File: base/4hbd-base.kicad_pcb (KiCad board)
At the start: 2 copper layers, 155 parts, among them J13 Conn_01x08, J14 Conn_02x25_Odd_Even, J15 Conn_02x25_Odd_Even, Q1 irf540n, Q10 2N7002, Q2 irf540n, Q3 irf540n, Q4 irf540n, Q5 irf540n, Q6 irf540n, Q7 irf540n, Q8 irf540n, Q9 2N7002, U1 SI8640, U10 ADS7886, U11 MOCD217M, U12 MOCD217M, U13 MOCD217M, U14 AMS1117-5.0, U15 AMS1117-5.0, U16 AMS1117-3.3, U17 LM2596S-ADJ, U18 AM26LV32, U19 LM2596S-ADJ, U2 SI8640, U20 AMS1117-5.0, U21 SN65HVD230, U3 IR2181, U4 IR2181, U5 IR2181, U6 IR2181, U7 ACS712xLCTR-30A, U8 ACS712xLCTR-30A, U9 ADS7886

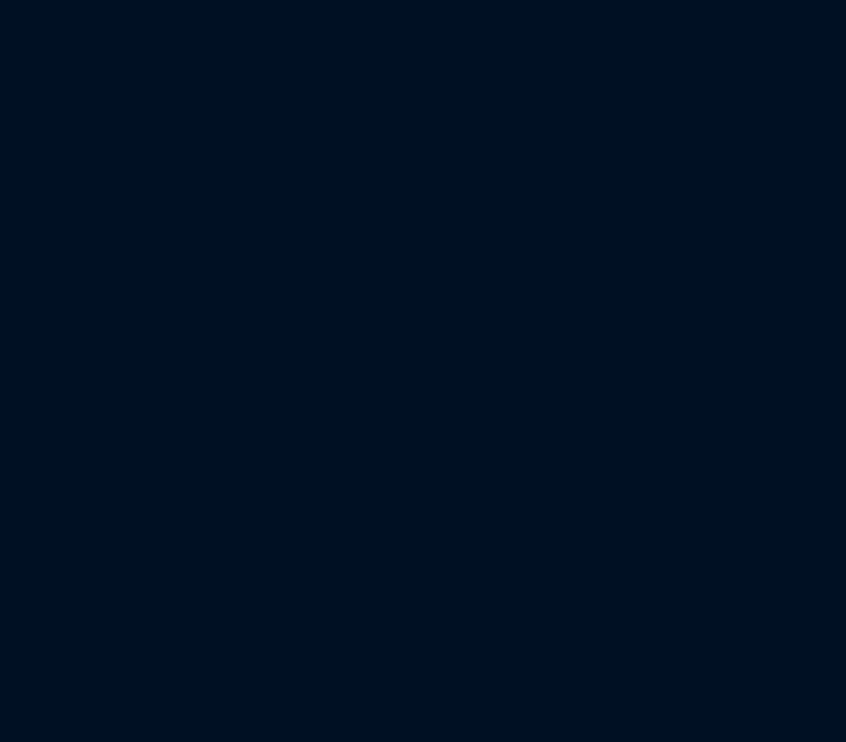
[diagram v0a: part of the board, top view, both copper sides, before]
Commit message: added footprints, created netlist
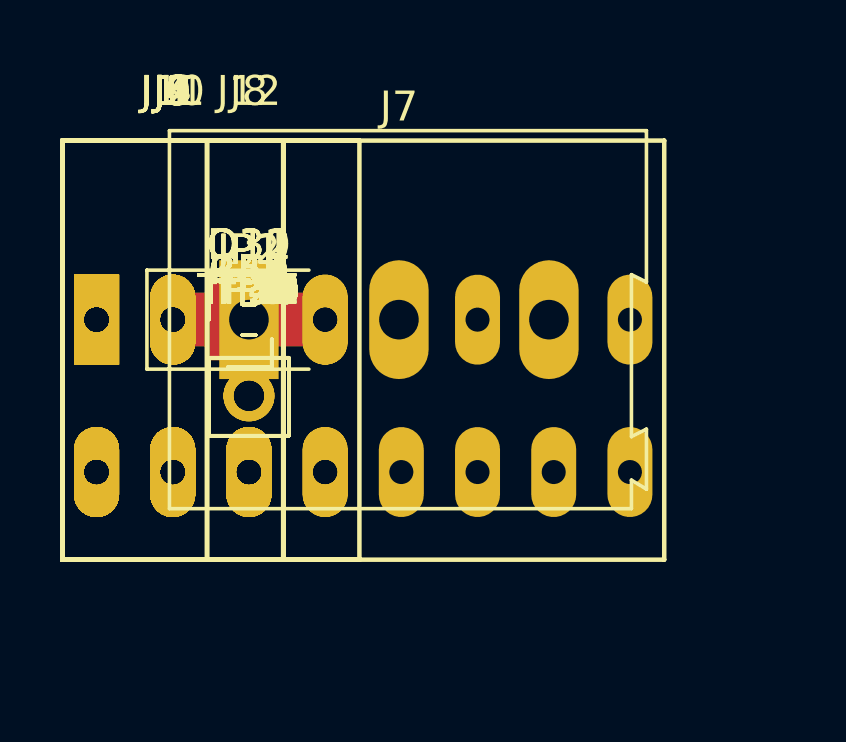
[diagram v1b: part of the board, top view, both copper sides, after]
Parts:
- added C42, C43: 0.1uF, Capacitor_SMD:C_0603_1608Metric, F.Cu at (0.00, 0.00)
- added D30: 1N5822, Diode_SMD:D_SMA, F.Cu at (0.00, 0.00)
- added D31: NUP2105L, Package_TO_SOT_SMD:SOT-23, F.Cu at (0.00, 0.00)
- added J1, J10, J11, J2, J3, J4, J9: Spring_Terminal_Connector_01x03, TerminalBlock:SpringTerminalBlock_KF141R_3_P2.54mm, F.Cu at (0.00, 0.00)
- added J12: Spring_Terminal_Connector_01x08, TerminalBlock:SpringTerminalBlock_KF141R_8_P2.54mm, F.Cu at (0.00, 0.00)
- added J5, J6: Spring_Terminal_Connector_01x02, TerminalBlock:SpringTerminalBlock_KF141R_2_P2.54mm, F.Cu at (0.00, 0.00)
- added J7: Screw_Terminal_01x03, TerminalBlock:TerminalBlock_Altech_AK300-3_P5.00mm, F.Cu at (0.00, 0.00)
- added J8: Spring_Terminal_Connector_01x04, TerminalBlock:SpringTerminalBlock_KF141R_4_P2.54mm, F.Cu at (0.00, 0.00)
- added JP1, JP2: Jumper_NC_Small, Connector_PinHeader_2.54mm:PinHeader_1x02_P2.54mm_Vertical, F.Cu at (0.00, 0.00)
- added Q11: 2N7002, Package_TO_SOT_SMD:SOT-23, F.Cu at (0.00, 0.00)
- added Q12: IRLML2060TRPBF, Package_TO_SOT_SMD:SOT-23, F.Cu at (0.00, 0.00)
- added R44: 10k, Resistor_SMD:R_0603_1608Metric, F.Cu at (0.00, 0.00)
- added R45: 2K2, Resistor_SMD:R_0603_1608Metric, F.Cu at (0.00, 0.00)
- added R46, R51: 10K, Resistor_SMD:R_0603_1608Metric, F.Cu at (0.00, 0.00)
- added R47, R48, R49, R54, R55: 120, Resistor_SMD:R_0603_1608Metric, F.Cu at (0.00, 0.00)
- added R50: 1K, Resistor_SMD:R_0603_1608Metric, F.Cu at (0.00, 0.00)
- added R52: 360, Resistor_SMD:R_0603_1608Metric, F.Cu at (0.00, 0.00)
- added R53: 100, Resistor_SMD:R_0603_1608Metric, F.Cu at (0.00, 0.00)
- added TP1, TP2, TP3, TP4, TP5: GNDp, TestPoint:TestPoint_Pad_D1.5mm, F.Cu at (0.00, 0.00)
- added TP10: PWM1p, TestPoint:TestPoint_Pad_D1.5mm, F.Cu at (0.00, 0.00)
- added TP11: PWM1n, TestPoint:TestPoint_Pad_D1.5mm, F.Cu at (0.00, 0.00)
- added TP12: PWM2p, TestPoint:TestPoint_Pad_D1.5mm, F.Cu at (0.00, 0.00)
- added TP13: PWM2n, TestPoint:TestPoint_Pad_D1.5mm, F.Cu at (0.00, 0.00)
- added TP14: PWM3p, TestPoint:TestPoint_Pad_D1.5mm, F.Cu at (0.00, 0.00)
- added TP15: PWM3n, TestPoint:TestPoint_Pad_D1.5mm, F.Cu at (0.00, 0.00)
- added TP16, TP17, TP18, TP19, TP20: GNDd, TestPoint:TestPoint_Pad_D1.5mm, F.Cu at (0.00, 0.00)
- added TP27: driver_VB, TestPoint:TestPoint_Pad_D1.5mm, F.Cu at (0.00, 0.00)
- added TP28: driver_VS, TestPoint:TestPoint_Pad_D1.5mm, F.Cu at (0.00, 0.00)
- added TP29: driver_HO, TestPoint:TestPoint_Pad_D1.5mm, F.Cu at (0.00, 0.00)
- added TP30: +24Vd_IN, TestPoint:TestPoint_Pad_D1.5mm, F.Cu at (0.00, 0.00)
- added TP31: +5Vd_main, TestPoint:TestPoint_Pad_D1.5mm, F.Cu at (0.00, 0.00)
- added TP32: +5Vd_enc, TestPoint:TestPoint_Pad_D1.5mm, F.Cu at (0.00, 0.00)
- added TP33: +24Vd_OUT, TestPoint:TestPoint_Pad_D1.5mm, F.Cu at (0.00, 0.00)
- added TP34: +6.8Vd, TestPoint:TestPoint_Pad_D1.5mm, F.Cu at (0.00, 0.00)
- added TP35: +24Vp_IN, TestPoint:TestPoint_Pad_D1.5mm, F.Cu at (0.00, 0.00)
- added TP36: +12Vp, TestPoint:TestPoint_Pad_D1.5mm, F.Cu at (0.00, 0.00)
- added TP37: +5Vp, TestPoint:TestPoint_Pad_D1.5mm, F.Cu at (0.00, 0.00)
- added TP38: CAN_Tx, TestPoint:TestPoint_Pad_D1.5mm, F.Cu at (0.00, 0.00)
- added TP39: CAN_Rx, TestPoint:TestPoint_Pad_D1.5mm, F.Cu at (0.00, 0.00)
- added TP40: 485_Tx, TestPoint:TestPoint_Pad_D1.5mm, F.Cu at (0.00, 0.00)
- added TP41: 485_Rx, TestPoint:TestPoint_Pad_D1.5mm, F.Cu at (0.00, 0.00)
- added TP42: 485_TxEn, TestPoint:TestPoint_Pad_D1.5mm, F.Cu at (0.00, 0.00)
- added TP6: Csen_0, TestPoint:TestPoint_Pad_D1.5mm, F.Cu at (0.00, 0.00)
- added TP7: Csen_1, TestPoint:TestPoint_Pad_D1.5mm, F.Cu at (0.00, 0.00)
- added TP8: PWM0p, TestPoint:TestPoint_Pad_D1.5mm, F.Cu at (0.00, 0.00)
- added TP9: PWM0n, TestPoint:TestPoint_Pad_D1.5mm, F.Cu at (0.00, 0.00)
- C19, C20, C21: value 22uF 10V -> 0.1uF
- C22: value 3.3nF 50V -> 22uF 10V
- C23: value 220uF 35V -> 22uF 10V
- C24: value 22uF 6.3V -> 3.3nF 50V
- C25: value 22uF 6.3V -> 220uF 35V
- C27: value 4.7uF 6.3V -> 22uF 6.3V
- C36: value 3.3nF 50V -> 0.1uF
- C37: value 100uF 35V -> 3.3nF 50V
- C38: value 100uF 16V -> 100uF 35V
- C39: value 220uF 10V -> 100uF 16V
- C40: value 4.7uF 6.3V -> 220uF 10V
- C41: value 0.1uF -> 4.7uF 6.3V
- D21: value 1N5822 -> BZT52C3V3
- D22: value SMBJ30CA -> BZT52C3V3
- D23: value BZT52C30 -> 1N5822
- D24: value 1N5822 -> SMBJ30CA
- D25: value BZT52C9V1 -> BZT52C30
- D27: value SMBJ30CA -> BZT52C9V1
- D29: value NUP2105L -> SMBJ30CA
- J13: value Conn_01x08 -> Screw_Terminal_01x02
- R17, R18: value 33 -> 360
- R21, R22: value 360 -> 33
- R35: value 2K2 -> 10k termistor
- R36: value 10K -> 10k termistor
- R37, R38, R39: value 120 -> 10k
- R40: value 1K -> 1k
- R41: value 10K -> 10
- R42: value 360 -> 10k
- R43: value 100 -> 1k
- U16: value AMS1117-3.3 -> LM2596S-ADJ
- U17: value LM2596S-ADJ -> AM26LV32
- U18: value AM26LV32 -> LM2596S-ADJ
- U19: value LM2596S-ADJ -> AMS1117-5.0
- U20: value AMS1117-5.0 -> SN65HVD230
- U21: value SN65HVD230 -> MAX485CSA
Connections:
- net /MCU/FPGA connection/SPI0_MOSI renamed Net-(J14-Pad32)
- net /MCU/FPGA connection/SPI1_MOSI renamed Net-(J15-Pad4)
- C19 pad 1: /Digital DC/DC/+6.8V -> /TempSens/Fan/TempAnalog
- C20 pad 1: /Digital DC/DC/+6.8V -> /TempSens/Fan/TempAnalog_2
- C21 pad 1: /Digital DC/DC/+6.8V -> /MCU/FPGA connection/Vsense2
- C22 pad 1: Net-(C22-Pad1) -> /Digital DC/DC/+6.8V
- C23 pad 1: Net-(C22-Pad1) -> /Digital DC/DC/+6.8V
- C24 pad 1: /CAN/RS485/+5V -> Net-(C24-Pad1)
- C25 pad 1: /Digital DC/DC/+5VEnc -> Net-(C24-Pad1)
- C26 pad 1: +3V3 -> /CAN/RS485/+5V
- C27 pad 1: /CAN/RS485/+5V -> /Digital DC/DC/+5VEnc
- C28 pad 1: /Digital DC/DC/+5VEnc -> /CAN/RS485/+5V
- C29 pad 1: +3V3 -> /Digital DC/DC/+5VEnc
- C36 pad 1: Net-(C36-Pad1) -> +3V3
- C36 pad 2: GNDPWR -> GND
- C37 pad 1: Net-(C36-Pad1) -> Net-(C37-Pad1)
- C38 pad 1: /DIO/+12V -> Net-(C37-Pad1)
- C39 pad 1: /MOSFETs/CurSense/Isolation/+5Vpwr -> /DIO/+12V
- C41 pad 1: +3V3 -> /MOSFETs/CurSense/Isolation/+5Vpwr
- C41 pad 2: GND -> GNDPWR
- D21 pad 1: Net-(D21-Pad1) -> /MCU/FPGA connection/Vsense2
- D21 pad 2: /Digital DC/DC/+24VD -> GND
- D22 pad 1: Net-(C22-Pad1) -> /MCU/FPGA connection/Pulse
- D23 pad 1: Net-(C30-Pad1) -> Net-(D23-Pad1)
- D23 pad 2: GND -> /Digital DC/DC/+24VD
- D24 pad 1: Net-(D24-Pad1) -> Net-(C24-Pad1)
- D25 pad 1: Net-(C33-Pad1) -> Net-(C30-Pad1)
- D26 pad 1: Net-(C36-Pad1) -> Net-(D26-Pad1)
- D26 pad 2: /Power DC/DC/+24VP -> GND
- D27 pad 1: Net-(C36-Pad1) -> Net-(C33-Pad1)
- D27 pad 2: GNDPWR -> GND
- D28 pad 1: Net-(D28-Pad1) -> Net-(C37-Pad1)
- D28 pad 2: GNDPWR -> /Power DC/DC/+24VP
- D29 pad 1: /CAN/RS485/CAN_L -> Net-(C37-Pad1)
- D29 pad 2: /CAN/RS485/CAN_H -> GNDPWR
- D29 pad 3: GND -> (no net)
- F3 pad 1: Net-(C22-Pad1) -> Net-(C24-Pad1)
- F3 pad 2: Net-(D21-Pad1) -> Net-(D23-Pad1)
- J13 pad 1: /Digital DC/DC/+5VEnc -> /Digital DC/DC/+24VD
- J13 pad 3: /Encoder Interface/EncA+ -> (no net)
- J13 pad 4: /Encoder Interface/EncA- -> (no net)
- J13 pad 5: /Encoder Interface/EncB+ -> (no net)
- J13 pad 6: /Encoder Interface/EncB- -> (no net)
- J13 pad 7: /Encoder Interface/EncZ+ -> (no net)
- J13 pad 8: /Encoder Interface/EncZ- -> (no net)
- J14 pad 11: /MCU/FPGA connection/+3.3V -> +3V3
- J14 pad 19: /MCU/FPGA connection/+3.3V -> +3V3
- J14 pad 22: /MCU/FPGA connection/+3.3V -> +3V3
- J14 pad 28: /MCU/FPGA connection/+3.3V -> +3V3
- J14 pad 36: /TempSens/Fan/Vsense -> /TempSens/Fan/TempAnalog_2
- J15 pad 23: /MCU/FPGA connection/+3.3V -> +3V3
- J15 pad 25: /MCU/FPGA connection/+3.3V -> +3V3
- J15 pad 50: /MCU/FPGA connection/+3.3V -> +3V3
- L1 pad 1: Net-(C22-Pad1) -> Net-(C24-Pad1)
- L3 pad 1: Net-(D24-Pad1) -> Net-(D26-Pad1)
- L5 pad 1: Net-(D28-Pad1) -> Net-(D30-Pad1)
- Q10 pad 1: Net-(D18-Pad2) -> Net-(D17-Pad2)
- Q10 pad 3: Net-(D20-Pad1) -> Net-(D19-Pad1)
- Q9 pad 1: Net-(D17-Pad2) -> Net-(Q9-Pad1)
- Q9 pad 2: GNDPWR -> Net-(Q9-Pad2)
- Q9 pad 3: Net-(D19-Pad1) -> Net-(Q9-Pad3)
- R17 pad 1: Net-(R17-Pad1) -> /MCU/FPGA connection/ADC_Csens0
- R17 pad 2: /MCU/FPGA connection/SPI0_CSn -> Net-(R17-Pad2)
- R18 pad 1: Net-(R18-Pad1) -> /MCU/FPGA connection/ADC_Csens1
- R18 pad 2: /MCU/FPGA connection/SPI0_SCK -> Net-(R18-Pad2)
- R19 pad 2: /MCU/FPGA connection/SPI1_CSn -> /MCU/FPGA connection/SPI0_CSn
- R20 pad 2: /MCU/FPGA connection/SPI1_SCK -> /MCU/FPGA connection/SPI0_SCK
- R21 pad 1: /MCU/FPGA connection/ADC_Csens0 -> Net-(R21-Pad1)
- R21 pad 2: Net-(R21-Pad2) -> /MCU/FPGA connection/SPI1_CSn
- R22 pad 1: /MCU/FPGA connection/ADC_Csens1 -> Net-(R22-Pad1)
- R22 pad 2: Net-(R22-Pad2) -> /MCU/FPGA connection/SPI1_SCK
- R35 pad 1: Net-(R35-Pad1) -> /TempSens/Fan/TempAnalog
- R35 pad 2: GND -> +3V3
- R36 pad 1: Net-(R35-Pad1) -> /TempSens/Fan/TempAnalog_2
- R36 pad 2: Net-(C33-Pad1) -> +3V3
- R37 pad 1: /Encoder Interface/EncA- -> /MCU/FPGA connection/Vsense2
- R37 pad 2: /Encoder Interface/EncA+ -> /Digital DC/DC/+Vpp
- R38 pad 1: /Encoder Interface/EncB- -> /TempSens/Fan/TempAnalog
- R38 pad 2: /Encoder Interface/EncB+ -> GND
- R39 pad 1: /Encoder Interface/EncZ- -> /TempSens/Fan/TempAnalog_2
- R39 pad 2: /Encoder Interface/EncZ+ -> GND
- R40 pad 1: Net-(R40-Pad1) -> /MCU/FPGA connection/Vsense2
- R40 pad 2: Net-(R40-Pad2) -> GND
- R41 pad 1: Net-(R40-Pad1) -> Net-(Q12-Pad1)
- R41 pad 2: /DIO/+12V -> /MCU/FPGA connection/PWM
- R42 pad 1: Net-(R40-Pad2) -> /TempSens/Fan/FAN_PWR
- R42 pad 2: GNDPWR -> Net-(Q12-Pad1)
- R43 pad 1: Net-(R43-Pad1) -> /MCU/FPGA connection/Pulse
- R43 pad 2: GND -> /TempSens/Fan/FAN_PULSE
- U10 pad 1: Net-(R22-Pad2) -> Net-(R18-Pad2)
- U10 pad 4: Net-(R20-Pad1) -> Net-(R22-Pad1)
- U10 pad 6: Net-(R19-Pad1) -> Net-(R21-Pad1)
- U16 pad 1: GND -> /Digital DC/DC/+Vpp
- U16 pad 2: +3V3 -> Net-(D26-Pad1)
- U16 pad 3: /Digital DC/DC/+6.8V -> GND
- U16 pad 4: (no net) -> Net-(R45-Pad1)
- U17 pad 1: /Digital DC/DC/+Vpp -> /Encoder Interface/EncA-
- U17 pad 2: Net-(D24-Pad1) -> /Encoder Interface/EncA+
- U17 pad 3: GND -> /Encoder Interface/EncA
- U17 pad 4: Net-(R35-Pad1) -> +3V3
- U17 pad 5: GND -> /Encoder Interface/EncB
- U18 pad 1: /Encoder Interface/EncA- -> Net-(C37-Pad1)
- U18 pad 10: /Encoder Interface/EncZ+ -> (no net)
- U18 pad 11: /Encoder Interface/EncZ -> (no net)
- U18 pad 12: Net-(U18-Pad12) -> (no net)
- U18 pad 13: Net-(U18-Pad13) -> (no net)
- U18 pad 14: Net-(U18-Pad14) -> (no net)
- U18 pad 16: +3V3 -> (no net)
- U18 pad 2: /Encoder Interface/EncA+ -> Net-(D30-Pad1)
- U18 pad 3: /Encoder Interface/EncA -> GNDPWR
- U18 pad 4: +3V3 -> Net-(R50-Pad1)
- U18 pad 5: /Encoder Interface/EncB -> GNDPWR
- U18 pad 6: /Encoder Interface/EncB+ -> (no net)
- U18 pad 7: /Encoder Interface/EncB- -> (no net)
- U18 pad 8: GND -> (no net)
- U18 pad 9: /Encoder Interface/EncZ- -> (no net)
- U19 pad 1: Net-(C36-Pad1) -> GNDPWR
- U19 pad 2: Net-(D28-Pad1) -> /MOSFETs/CurSense/Isolation/+5Vpwr
- U19 pad 3: GNDPWR -> /DIO/+12V
- U19 pad 4: Net-(R40-Pad1) -> (no net)
- U19 pad 5: GNDPWR -> (no net)
- U20 pad 1: GNDPWR -> /CAN/RS485/CAN_TX
- U20 pad 2: /MOSFETs/CurSense/Isolation/+5Vpwr -> GND
- U20 pad 3: /DIO/+12V -> +3V3
- U20 pad 4: (no net) -> /CAN/RS485/CAN_RX
- U21 pad 1: /CAN/RS485/CAN_TX -> /CAN/RS485/RS485_TX
- U21 pad 2: GND -> /CAN/RS485/RS485_TXEN
- U21 pad 3: +3V3 -> /CAN/RS485/RS485_TXEN
- U21 pad 4: /CAN/RS485/CAN_RX -> /CAN/RS485/RS485_RX
- U21 pad 5: Net-(U21-Pad5) -> GND
- U21 pad 6: /CAN/RS485/CAN_L -> /CAN/RS485/RS485+
- U21 pad 7: /CAN/RS485/CAN_H -> /CAN/RS485/RS485-
- U21 pad 8: Net-(R43-Pad1) -> /CAN/RS485/+5V
- U7 pad 7: Net-(R21-Pad2) -> Net-(R17-Pad2)
- U8 pad 7: Net-(R22-Pad2) -> Net-(R18-Pad2)
- U9 pad 1: Net-(R21-Pad2) -> Net-(R17-Pad2)
- U9 pad 4: Net-(R18-Pad1) -> Net-(R20-Pad1)
- U9 pad 6: Net-(R17-Pad1) -> Net-(R19-Pad1)

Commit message: assign footprints
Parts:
- added TP21: SPI0_sck, TestPoint:TestPoint_Pad_D1.5mm, F.Cu at (0.00, 0.00)
- added TP22: SPI0_cs, TestPoint:TestPoint_Pad_D1.5mm, F.Cu at (0.00, 0.00)
- added TP23: SPI0_miso, TestPoint:TestPoint_Pad_D1.5mm, F.Cu at (0.00, 0.00)
- added TP24: SPI1_sck, TestPoint:TestPoint_Pad_D1.5mm, F.Cu at (0.00, 0.00)
- added TP25: SPI1_cs, TestPoint:TestPoint_Pad_D1.5mm, F.Cu at (0.00, 0.00)
- added TP26: SPI1_miso, TestPoint:TestPoint_Pad_D1.5mm, F.Cu at (0.00, 0.00)
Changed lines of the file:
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@@
 (kicad_pcb (version 4) (host pcbnew 4.0.2+dfsg1-stable)
   (general
-    (links 497)
-    (no_connects 278)
+    (links 503)
+    (no_connects 284)
     (area 0 0 0 0)
     (thickness 1.6)
@@
     (tracks 0)
     (zones 0)
-    (modules 223)
+    (modules 229)
     (nets 193)
   )
@@
     (attr virtual)
     (fp_text reference TP34 (at 0 -1) (layer F.SilkS)
-      (effects (font (size 1 1)))
+      (effects (font (size 1 1) (thickness 0.15)))
     )
     (fp_text value +6.8Vd (at 0 1) (layer F.Fab)
-      (effects (font (size 1 1)))
+      (effects (font (size 1 1) (thickness 0.15)))
     )
     (fp_text user %R (at 0 -1) (layer F.Fab)
-      (effects (font (size 1 1)))
+      (effects (font (size 1 1) (thickness 0.15)))
     )
     (fp_circle (center 0 0) (end 1 0) (layer F.CrtYd) (width 0))
@@
     (attr virtual)
     (fp_text reference TP38 (at 0 -1) (layer F.SilkS)
-      (effects (font (size 1 1)))
+      (effects (font (size 1 1) (thickness 0.15)))
     )
     (fp_text value CAN_Tx (at 0 1) (layer F.Fab)
-      (effects (font (size 1 1)))
+      (effects (font (size 1 1) (thickness 0.15)))
     )
     (fp_text user %R (at 0 -1) (layer F.Fab)
-      (effects (font (size 1 1)))
+      (effects (font (size 1 1) (thickness 0.15)))
     )
     (fp_circle (center 0 0) (end 1 0) (layer F.CrtYd) (width 0))
@@
     (attr virtual)
     (fp_text reference TP39 (at 0 -1) (layer F.SilkS)
-      (effects (font (size 1 1)))
+      (effects (font (size 1 1) (thickness 0.15)))
     )
     (fp_text value CAN_Rx (at 0 1) (layer F.Fab)
-      (effects (font (size 1 1)))
+      (effects (font (size 1 1) (thickness 0.15)))
     )
     (fp_text user %R (at 0 -1) (layer F.Fab)
-      (effects (font (size 1 1)))
+      (effects (font (size 1 1) (thickness 0.15)))
     )
     (fp_circle (center 0 0) (end 1 0) (layer F.CrtYd) (width 0))
@@
     (attr virtual)
     (fp_text reference TP40 (at 0 -1) (layer F.SilkS)
-      (effects (font (size 1 1)))
+      (effects (font (size 1 1) (thickness 0.15)))
     )
     (fp_text value 485_Tx (at 0 1) (layer F.Fab)
-      (effects (font (size 1 1)))
+      (effects (font (size 1 1) (thickness 0.15)))
     )
     (fp_text user %R (at 0 -1) (layer F.Fab)
-      (effects (font (size 1 1)))
+      (effects (font (size 1 1) (thickness 0.15)))
     )
     (fp_circle (center 0 0) (end 1 0) (layer F.CrtYd) (width 0))
@@
     (attr virtual)
     (fp_text reference TP41 (at 0 -1) (layer F.SilkS)
-      (effects (font (size 1 1)))
+      (effects (font (size 1 1) (thickness 0.15)))
     )
     (fp_text value 485_Rx (at 0 1) (layer F.Fab)
-      (effects (font (size 1 1)))
+      (effects (font (size 1 1) (thickness 0.15)))
     )
     (fp_text user %R (at 0 -1) (layer F.Fab)
-      (effects (font (size 1 1)))
+      (effects (font (size 1 1) (thickness 0.15)))
     )
     (fp_circle (center 0 0) (end 1 0) (layer F.CrtYd) (width 0))
@@
     (attr virtual)
     (fp_text reference TP42 (at 0 -1) (layer F.SilkS)
-      (effects (font (size 1 1)))
+      (effects (font (size 1 1) (thickness 0.15)))
     )
     (fp_text value 485_TxEn (at 0 1) (layer F.Fab)
-      (effects (font (size 1 1)))
+      (effects (font (size 1 1) (thickness 0.15)))
     )
     (fp_text user %R (at 0 -1) (layer F.Fab)
-      (effects (font (size 1 1)))
+      (effects (font (size 1 1) (thickness 0.15)))
     )
     (fp_circle (center 0 0) (end 1 0) (layer F.CrtYd) (width 0))
@@
       (net 125 /CAN/RS485/RS485_TXEN))
   )
+  (module TestPoint:TestPoint_Pad_D1.5mm (layer F.Cu)
+    (at 0 0)
+    (descr "SMD pad as test Point, diameter 1.5mm")
+    (tags "test point SMD pad")
+    (attr virtual)
+    (fp_text reference TP21 (at 0 -1.648) (layer F.SilkS)
+      (effects (font (size 1 1) (thickness 0.15)))
+    )
+    (fp_text value SPI0_sck (at 0 1.75) (layer F.Fab)
+      (effects (font (size 1 1) (thickness 0.15)))
+    )
+    (fp_text user %R (at 0 -1.65) (layer F.Fab)
+      (effects (font (size 1 1) (thickness 0.15)))
+    )
+    (fp_circle (center 0 0) (end 1.25 0) (layer F.CrtYd) (width 0.05))
+    (fp_circle (center 0 0) (end 0 0.95) (layer F.SilkS) (width 0.12))
+    (pad 1 smd circle (at 0 0) (size 1.5 1.5) (layers F.Cu F.Mask)
+      (net 72 "/MCU/FPGA connection/SPI0_SCK"))
+  )
+  (module TestPoint:TestPoint_Pad_D1.5mm (layer F.Cu)
+    (at 0 0)
+    (descr "SMD pad as test Point, diameter 1.5mm")
+    (tags "test point SMD pad")
+    (attr virtual)
+    (fp_text reference TP22 (at 0 -1.648) (layer F.SilkS)
+      (effects (font (size 1 1) (thickness 0.15)))
+    )
+    (fp_text value SPI0_cs (at 0 1.75) (layer F.Fab)
+      (effects (font (size 1 1) (thickness 0.15)))
+    )
+    (fp_text user %R (at 0 -1.65) (layer F.Fab)
+      (effects (font (size 1 1) (thickness 0.15)))
+    )
+    (fp_circle (center 0 0) (end 1.25 0) (layer F.CrtYd) (width 0.05))
+    (fp_circle (center 0 0) (end 0 0.95) (layer F.SilkS) (width 0.12))
+    (pad 1 smd circle (at 0 0) (size 1.5 1.5) (layers F.Cu F.Mask)
+      (net 71 "/MCU/FPGA connection/SPI0_CSn"))
+  )
+  (module TestPoint:TestPoint_Pad_D1.5mm (layer F.Cu)
+    (at 0 0)
+    (descr "SMD pad as test Point, diameter 1.5mm")
+    (tags "test point SMD pad")
+    (attr virtual)
+    (fp_text reference TP23 (at 0 -1.648) (layer F.SilkS)
+      (effects (font (size 1 1) (thickness 0.15)))
+    )
+    (fp_text value SPI0_miso (at 0 1.75) (layer F.Fab)
+      (effects (font (size 1 1) (thickness 0.15)))
+    )
+    (fp_text user %R (at 0 -1.65) (layer F.Fab)
+      (effects (font (size 1 1) (thickness 0.15)))
+    )
+    (fp_circle (center 0 0) (end 1.25 0) (layer F.CrtYd) (width 0.05))
+    (fp_circle (center 0 0) (end 0 0.95) (layer F.SilkS) (width 0.12))
+    (pad 1 smd circle (at 0 0) (size 1.5 1.5) (layers F.Cu F.Mask)
+      (net 73 "/MCU/FPGA connection/SPI0_MISO"))
+  )
+  (module TestPoint:TestPoint_Pad_D1.5mm (layer F.Cu)
+    (at 0 0)
+    (descr "SMD pad as test Point, diameter 1.5mm")
+    (tags "test point SMD pad")
+    (attr virtual)
+    (fp_text reference TP24 (at 0 -1.648) (layer F.SilkS)
+      (effects (font (size 1 1) (thickness 0.15)))
+    )
+    (fp_text value SPI1_sck (at 0 1.75) (layer F.Fab)
+      (effects (font (size 1 1) (thickness 0.15)))
+    )
+    (fp_text user %R (at 0 -1.65) (layer F.Fab)
+      (effects (font (size 1 1) (thickness 0.15)))
+    )
+    (fp_circle (center 0 0) (end 1.25 0) (layer F.CrtYd) (width 0.05))
+    (fp_circle (center 0 0) (end 0 0.95) (layer F.SilkS) (width 0.12))
+    (pad 1 smd circle (at 0 0) (size 1.5 1.5) (layers F.Cu F.Mask)
+      (net 90 "/MCU/FPGA connection/SPI1_SCK"))
+  )
+  (module TestPoint:TestPoint_Pad_D1.5mm (layer F.Cu)
+    (at 0 0)
+    (descr "SMD pad as test Point, diameter 1.5mm")
+    (tags "test point SMD pad")
+    (attr virtual)
+    (fp_text reference TP25 (at 0 -1.648) (layer F.SilkS)
+      (effects (font (size 1 1) (thickness 0.15)))
+    )
+    (fp_text value SPI1_cs (at 0 1.75) (layer F.Fab)
+      (effects (font (size 1 1) (thickness 0.15)))
+    )
+    (fp_text user %R (at 0 -1.65) (layer F.Fab)
+      (effects (font (size 1 1) (thickness 0.15)))
+    )
+    (fp_circle (center 0 0) (end 1.25 0) (layer F.CrtYd) (width 0.05))
+    (fp_circle (center 0 0) (end 0 0.95) (layer F.SilkS) (width 0.12))
+    (pad 1 smd circle (at 0 0) (size 1.5 1.5) (layers F.Cu F.Mask)
+      (net 89 "/MCU/FPGA connection/SPI1_CSn"))
+  )
+  (module TestPoint:TestPoint_Pad_D1.5mm (layer F.Cu)
+    (at 0 0)
+    (descr "SMD pad as test Point, diameter 1.5mm")
+    (tags "test point SMD pad")
+    (attr virtual)
+    (fp_text reference TP26 (at 0 -1.648) (layer F.SilkS)
+      (effects (font (size 1 1) (thickness 0.15)))
+    )
+    (fp_text value SPI1_miso (at 0 1.75) (layer F.Fab)
+      (effects (font (size 1 1) (thickness 0.15)))
+    )
+    (fp_text user %R (at 0 -1.65) (layer F.Fab)
+      (effects (font (size 1 1) (thickness 0.15)))
+    )
+    (fp_circle (center 0 0) (end 1.25 0) (layer F.CrtYd) (width 0.05))
+    (fp_circle (center 0 0) (end 0 0.95) (layer F.SilkS) (width 0.12))
+    (pad 1 smd circle (at 0 0) (size 1.5 1.5) (layers F.Cu F.Mask)
+      (net 91 "/MCU/FPGA connection/SPI1_MISO"))
+  )
 )

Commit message: fix for pcb
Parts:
- added MK1, MK2, MK3, MK4: Mounting_Hole, MountingHole:MountingHole_3.5mm_Pad, F.Cu at (0.00, 0.00)
- C19, C20, C21: footprint Capacitor_Tantalum_SMD:CP_EIA-3216-18_Kemet-A -> Capacitor_SMD:C_0805_2012Metric
- C22, C27: footprint Capacitor_SMD:C_0603_1608Metric -> Capacitor_Tantalum_SMD:CP_EIA-3216-18_Kemet-A
- C23: footprint Capacitor_SMD:CP_Elec_8x10 -> Capacitor_Tantalum_SMD:CP_EIA-3216-18_Kemet-A
- C24: footprint Capacitor_Tantalum_SMD:CP_EIA-3216-18_Kemet-A -> Capacitor_SMD:C_0603_1608Metric
- C25: footprint Capacitor_Tantalum_SMD:CP_EIA-3216-18_Kemet-A -> Capacitor_SMD:CP_Elec_8x10
- C37: footprint Capacitor_SMD:CP_Elec_6.3x7.7 -> Capacitor_SMD:C_0603_1608Metric
- C38: footprint Capacitor_SMD:CP_Elec_6.3x5.3 -> Capacitor_SMD:CP_Elec_6.3x7.7
- C40: footprint Capacitor_SMD:C_0603_1608Metric -> Capacitor_SMD:CP_Elec_6.3x5.3
- D21: footprint Diode_SMD:D_SMA -> Diode_SMD:D_SOD-123
- D22, D27: footprint Diode_SMD:D_SMB -> Diode_SMD:D_SOD-123
- D23: footprint Diode_SMD:D_SOD-123 -> Diode_SMD:D_SMA
- D24: footprint Diode_SMD:D_SMA -> Diode_SMD:D_SMB
- D29: footprint Package_TO_SOT_SMD:SOT-23 -> Diode_SMD:D_SMB
- J13: footprint Connector_PinHeader_2.54mm:PinHeader_1x08_P2.54mm_Horizontal -> TerminalBlock:TerminalBlock_Altech_AK300-2_P5.00mm
- J8: value Spring_Terminal_Connector_01x04 -> Screw_Terminal_01x04; footprint TerminalBlock:SpringTerminalBlock_KF141R_4_P2.54mm -> TerminalBlock:TerminalBlock_Altech_AK300-4_P5.00mm
- R35, R36: footprint Resistor_SMD:R_0603_1608Metric -> Resistor_SMD:R_0805_2012Metric
- U16: footprint Package_TO_SOT_SMD:SOT-223 -> Package_TO_SOT_SMD:TO-263-5_TabPin3
- U17: footprint Package_TO_SOT_SMD:TO-263-5_TabPin3 -> Package_SOIC:SOIC-16_3.9x9.9mm_P1.27mm
- U18: footprint Package_SOIC:SOIC-16_3.9x9.9mm_P1.27mm -> Package_TO_SOT_SMD:TO-263-5_TabPin3
- U19: footprint Package_TO_SOT_SMD:TO-263-5_TabPin3 -> Package_TO_SOT_SMD:SOT-223
- U20: footprint Package_TO_SOT_SMD:SOT-223 -> Package_SOIC:SOIC-8_3.9x4.9mm_P1.27mm
- U21: footprint Package_SOIC:SOIC-8_3.9x4.9mm_P1.27mm -> Package_SOIC:SO-8_5.3x6.2mm_P1.27mm
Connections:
- J14 pad 1: Net-(J14-Pad1) -> (no net)
- J14 pad 12: Net-(J14-Pad12) -> (no net)
- J14 pad 13: Net-(J14-Pad13) -> (no net)
- J14 pad 14: Net-(J14-Pad14) -> (no net)
- J14 pad 16: Net-(J14-Pad16) -> (no net)
- J14 pad 18: Net-(J14-Pad18) -> (no net)
- J14 pad 2: Net-(J14-Pad2) -> (no net)
- J14 pad 20: Net-(J14-Pad20) -> (no net)
- J14 pad 21: Net-(J14-Pad21) -> (no net)
- J14 pad 26: Net-(J14-Pad26) -> (no net)
- J14 pad 3: Net-(J14-Pad3) -> (no net)
- J14 pad 32: Net-(J14-Pad32) -> (no net)
- J14 pad 35: Net-(J14-Pad35) -> (no net)
- J14 pad 37: Net-(J14-Pad37) -> (no net)
- J14 pad 4: Net-(J14-Pad4) -> (no net)
- J14 pad 46: /MCU/FPGA connection/PWM_Trip -> (no net)
- J14 pad 47: Net-(J14-Pad47) -> (no net)
- J14 pad 48: Net-(J14-Pad48) -> (no net)
- J14 pad 5: Net-(J14-Pad5) -> (no net)
- J14 pad 6: Net-(J14-Pad6) -> (no net)
- J14 pad 7: Net-(J14-Pad7) -> (no net)
- J14 pad 8: Net-(J14-Pad8) -> (no net)
- J14 pad 9: Net-(J14-Pad9) -> (no net)
- J15 pad 10: Net-(J15-Pad10) -> (no net)
- J15 pad 11: Net-(J15-Pad11) -> (no net)
- J15 pad 12: Net-(J15-Pad12) -> (no net)
- J15 pad 14: Net-(J15-Pad14) -> (no net)
- J15 pad 15: Net-(J15-Pad15) -> (no net)
- J15 pad 16: Net-(J15-Pad16) -> (no net)
- J15 pad 17: Net-(J15-Pad17) -> (no net)
- J15 pad 18: Net-(J15-Pad18) -> (no net)
- J15 pad 19: Net-(J15-Pad19) -> (no net)
- J15 pad 20: Net-(J15-Pad20) -> (no net)
- J15 pad 21: Net-(J15-Pad21) -> (no net)
- J15 pad 22: Net-(J15-Pad22) -> (no net)
- J15 pad 26: Net-(J15-Pad26) -> (no net)
- J15 pad 27: Net-(J15-Pad27) -> (no net)
- J15 pad 28: Net-(J15-Pad28) -> (no net)
- J15 pad 29: Net-(J15-Pad29) -> (no net)
- J15 pad 30: Net-(J15-Pad30) -> (no net)
- J15 pad 37: Net-(J15-Pad37) -> (no net)
- J15 pad 38: Net-(J15-Pad38) -> (no net)
- J15 pad 39: Net-(J15-Pad39) -> (no net)
- J15 pad 4: Net-(J15-Pad4) -> (no net)
- J15 pad 40: Net-(J15-Pad40) -> (no net)
- J15 pad 44: Net-(J15-Pad44) -> (no net)
- J15 pad 47: Net-(J15-Pad47) -> (no net)
- J15 pad 48: Net-(J15-Pad48) -> (no net)
- J15 pad 5: Net-(J15-Pad5) -> (no net)
- J15 pad 6: Net-(J15-Pad6) -> (no net)
- J15 pad 7: Net-(J15-Pad7) -> (no net)
- J15 pad 8: Net-(J15-Pad8) -> (no net)
- Q9 pad 1: Net-(Q9-Pad1) -> (no net)
- Q9 pad 2: Net-(Q9-Pad2) -> (no net)
- Q9 pad 3: Net-(Q9-Pad3) -> (no net)

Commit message: define board outline
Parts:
- moved R44 402.0 mm to (400.5, 34.7)
- moved TP37 401.6 mm to (387.5, 105.3)
- moved R50 400.1 mm to (388.7, 95.0)
- moved R52 399.8 mm to (387.0, 100.5)
- moved R51 398.9 mm to (388.7, 89.6)
- moved R55 398.7 mm to (377.5, 128.4)
- moved D30 396.9 mm to (381.5, 109.6)
- moved TP40 396.1 mm to (376.3, 123.6)
- moved R54 395.0 mm to (371.7, 133.8)
- moved TP41 394.9 mm to (376.4, 119.5)
- moved C42 394.8 mm to (373.4, 128.4)
- moved C43 392.2 mm to (367.6, 136.8)
- moved R53 389.8 mm to (367.0, 131.4)
- moved TP38 389.3 mm to (368.1, 126.6)
- moved D31 388.6 mm to (369.3, 121.0)
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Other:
- board outline added: 120 x 100 mm
